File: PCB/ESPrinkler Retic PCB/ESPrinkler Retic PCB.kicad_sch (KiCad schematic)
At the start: 0 parts

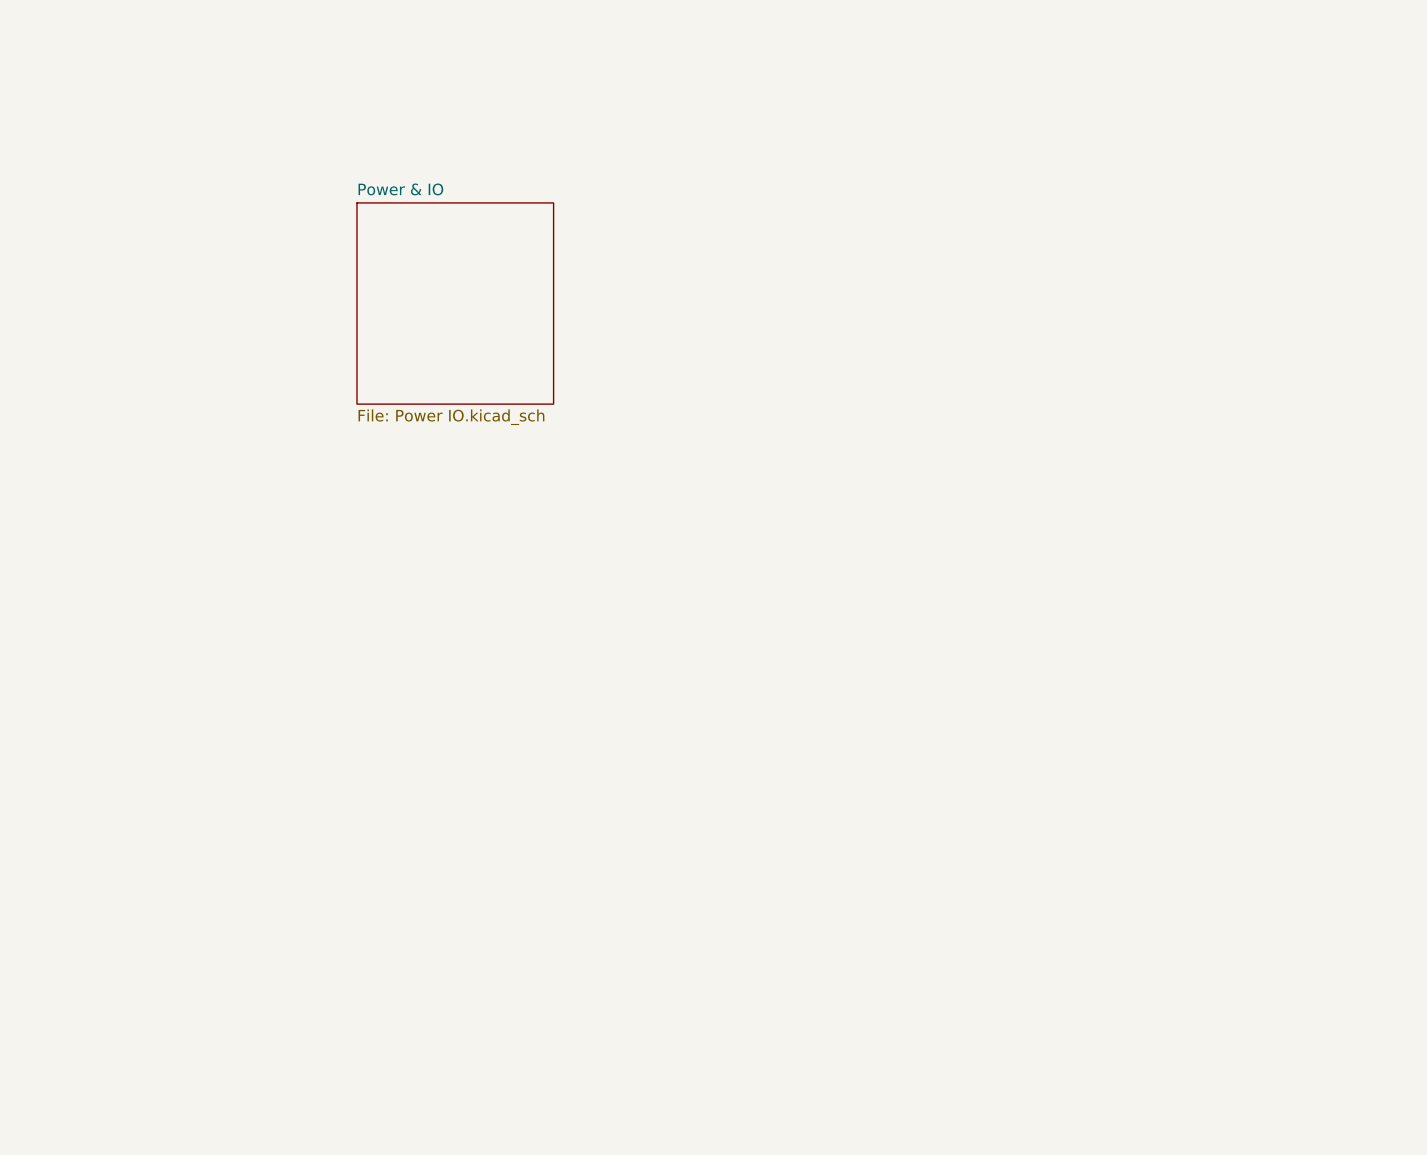
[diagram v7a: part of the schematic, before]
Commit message: Continued work migrating to multi-sheet design
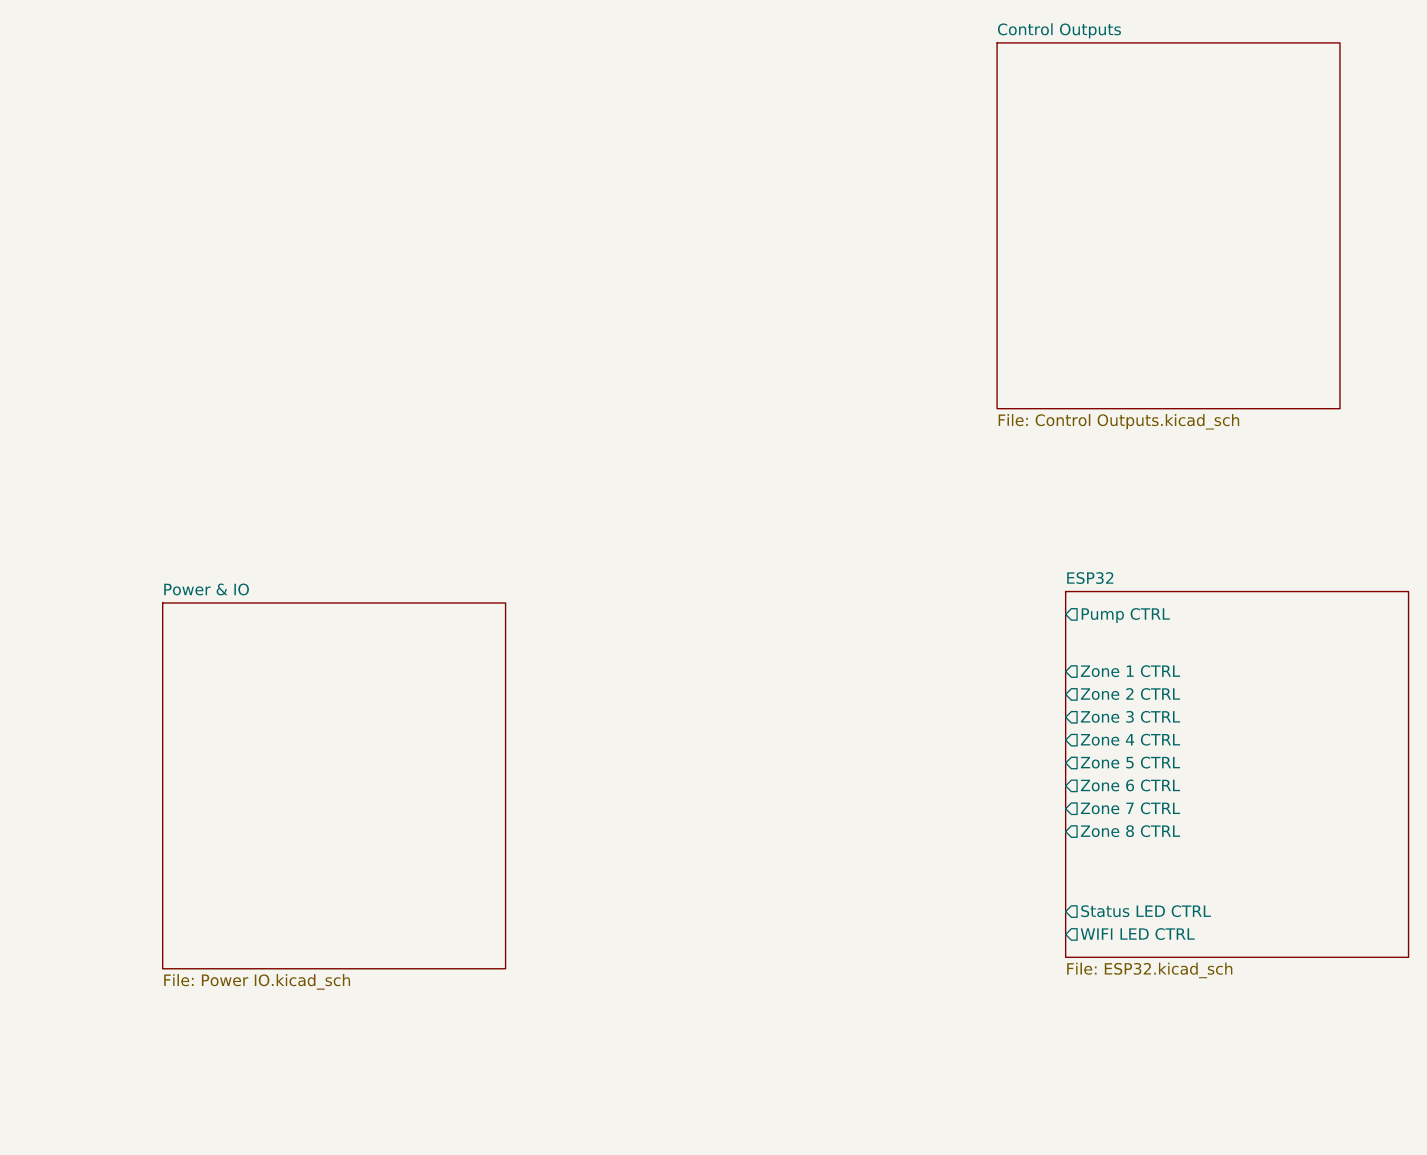
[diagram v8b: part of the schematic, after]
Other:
- added sheet Control Outputs (Control Outputs.kicad_sch)
- added sheet ESP32 (ESP32.kicad_sch)
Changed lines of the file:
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@@
 	)
 	(sheet
-		(at 76.2 50.8)
-		(size 21.844 22.352)
+		(at 54.61 95.25)
+		(size 38.1 40.64)
 		(exclude_from_sim no)
 		(in_bom yes)
@@
 		)
 		(fill
-			(color 0 0 0 0.0000)
+			(color 255 255 194 1.0000)
 		)
 		(property "Sheetname" "Power & IO"
-			(at 76.2 50.0884 0)
+			(at 54.61 94.5384 0)
 			(effects
 				(font
@@
 		)
 		(property "Sheetfile" "Power IO.kicad_sch"
-			(at 76.2 73.7366 0)
+			(at 54.61 136.4746 0)
 			(effects
 				(font
@@
 				)
 			)
+		)
+	)
+	(sheet
+		(at 147.32 33.02)
+		(size 38.1 40.64)
+		(exclude_from_sim no)
+		(in_bom yes)
+		(on_board yes)
+		(dnp no)
+		(fields_autoplaced yes)
+		(stroke
+			(width 0.1524)
+			(type solid)
+		)
+		(fill
+			(color 255 255 194 1.0000)
+		)
+		(property "Sheetname" "Control Outputs"
+			(at 147.32 32.3084 0)
+			(effects
+				(font
+					(size 1.27 1.27)
+				)
+				(justify left bottom)
+			)
+		)
+		(property "Sheetfile" "Control Outputs.kicad_sch"
+			(at 147.32 74.2446 0)
+			(effects
+				(font
+					(size 1.27 1.27)
+				)
+				(justify left top)
+			)
+		)
+		(instances
+			(project "ESPrinkler Retic PCB"
+				(path "/3c6b8bc3-d793-478e-a69e-22171e9bcb1b"
+					(page "3")
+				)
+			)
+		)
+	)
+	(sheet
+		(at 154.94 93.98)
+		(size 38.1 40.64)
+		(exclude_from_sim no)
+		(in_bom yes)
+		(on_board yes)
+		(dnp no)
+		(fields_autoplaced yes)
+		(stroke
+			(width 0.1524)
+			(type solid)
+		)
+		(fill
+			(color 255 255 194 1.0000)
+		)
+		(property "Sheetname" "ESP32"
+			(at 154.94 93.2684 0)
+			(effects
+				(font
+					(size 1.27 1.27)
+				)
+				(justify left bottom)
+			)
+		)
+		(property "Sheetfile" "ESP32.kicad_sch"
+			(at 154.94 135.2046 0)
+			(effects
+				(font
+					(size 1.27 1.27)
+				)
+				(justify left top)
+			)
+		)
+		(pin "Pump CTRL" output
+			(at 154.94 96.52 180)
+			(effects
+				(font
+					(size 1.27 1.27)
+				)
+				(justify left)
+			)
+		)
+		(pin "Status LED CTRL" output
+			(at 154.94 129.54 180)
+			(effects
+				(font
+					(size 1.27 1.27)
+				)
+				(justify left)
+			)
+		)
+		(pin "WIFI LED CTRL" output
+			(at 154.94 132.08 180)
+			(effects
+				(font
+					(size 1.27 1.27)
+				)
+				(justify left)
+			)
+		)
+		(pin "Zone 1 CTRL" output
+			(at 154.94 102.87 180)
+			(effects
+				(font
+					(size 1.27 1.27)
+				)
+				(justify left)
+			)
+		)
+		(pin "Zone 2 CTRL" output
+			(at 154.94 105.41 180)
+			(effects
+				(font
+					(size 1.27 1.27)
+				)
+				(justify left)
+			)
+		)
+		(pin "Zone 3 CTRL" output
+			(at 154.94 107.95 180)
+			(effects
+				(font
+					(size 1.27 1.27)
+				)
+				(justify left)
+			)
+		)
+		(pin "Zone 4 CTRL" output
+			(at 154.94 110.49 180)
+			(effects
+				(font
+					(size 1.27 1.27)
+				)
+				(justify left)
+			)
+		)
+		(pin "Zone 5 CTRL" output
+			(at 154.94 113.03 180)
+			(effects
+				(font
+					(size 1.27 1.27)
+				)
+				(justify left)
+			)
+		)
+		(pin "Zone 6 CTRL" output
+			(at 154.94 115.57 180)
+			(effects
+				(font
+					(size 1.27 1.27)
+				)
+				(justify left)
+			)
+		)
+		(pin "Zone 7 CTRL" output
+			(at 154.94 118.11 180)
+			(effects
+				(font
+					(size 1.27 1.27)
+				)
+				(justify left)
+			)
+		)
+		(pin "Zone 8 CTRL" output
+			(at 154.94 120.65 180)
+			(effects
+				(font
+					(size 1.27 1.27)
+				)
+				(justify left)
+			)
+		)
+		(instances
+			(project "ESPrinkler Retic PCB"
+				(path "/3c6b8bc3-d793-478e-a69e-22171e9bcb1b"
+					(page "4")
+				)
+			)
